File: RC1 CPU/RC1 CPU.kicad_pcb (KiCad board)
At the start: 2 copper layers, 99.1 x 99.1 mm, 51 parts, among them J1 Expansion, J2 RC1_UI_Port, J3 BARREL_JACK, M1 Mounting, M2 Mounting, M3 Mounting, M4 Mounting, U1 WD65C02, U2 HM62256BLP-7, U3 28C256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

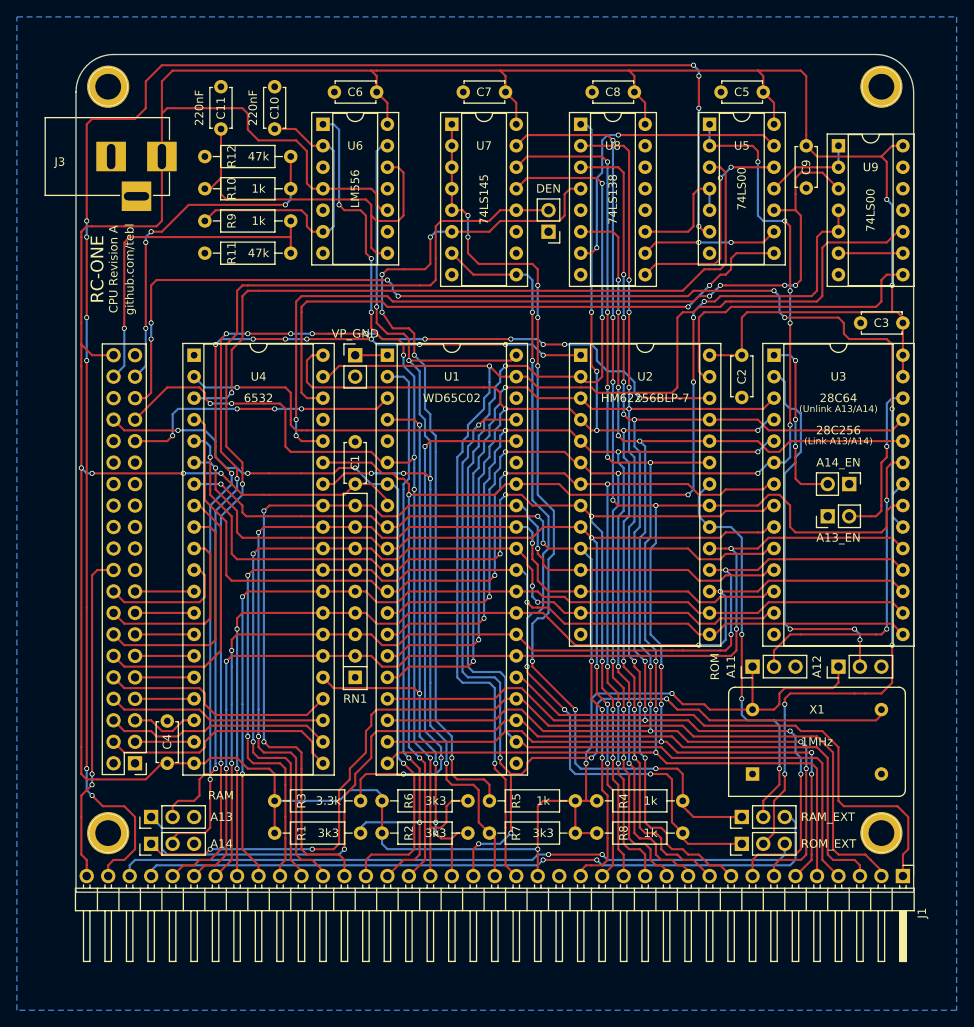
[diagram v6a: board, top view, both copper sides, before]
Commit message: Decided to connect remaining RAM address lines for external logic.
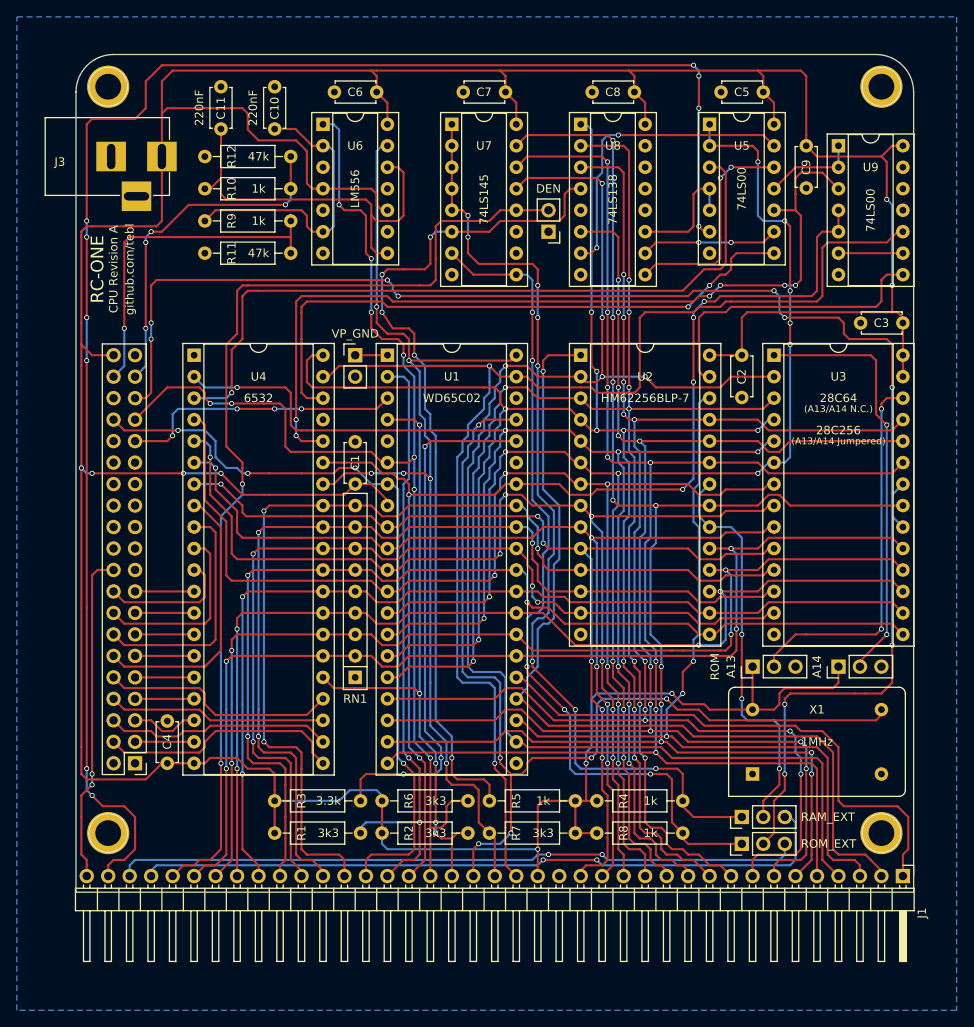
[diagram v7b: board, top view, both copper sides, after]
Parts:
- removed JP10: A14, Pin_Headers:Pin_Header_Straight_1x03_Pitch2.54mm
- removed JP5: A13_EN, Pin_Headers:Pin_Header_Straight_1x02_Pitch2.54mm
- removed JP6: A14_EN, Pin_Headers:Pin_Header_Straight_1x02_Pitch2.54mm
- removed JP9: A13, Pin_Headers:Pin_Header_Straight_1x03_Pitch2.54mm
- JP7: value A11 -> A13
- JP8: value A12 -> A14
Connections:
- JP7 pad 2: /A11_W -> Net-(JP7-Pad2)
- JP8 pad 2: /A12_W -> Net-(JP8-Pad2)
- U2 pad 1: /A14_RAM -> /A14
- U2 pad 26: /A13_RAM -> /A13
- U3 pad 1: Net-(JP6-Pad2) -> Net-(JP8-Pad2)
- U3 pad 2: /A12_W -> /A12
- U3 pad 23: /A11_W -> /A11
- U3 pad 26: Net-(JP5-Pad2) -> Net-(JP7-Pad2)
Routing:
- net /A13_RAM: track 125.3 -> 0.00 mm, vias 12 -> 0
- net /A14_RAM: track 108.8 -> 0.00 mm, vias 10 -> 0
- net Net-(JP8-Pad2): track 0.00 -> 50.4 mm, vias 0 -> 2
- net Net-(JP7-Pad2): track 0.00 -> 45.4 mm, vias 0 -> 2
- net /A12_W: track 45.3 -> 0.00 mm, vias 3 -> 0
- net /A11_W: track 38.1 -> 0.00 mm, vias 2 -> 0
- net /A11: track 158.7 -> 182.6 mm
- net /A12: track 148.2 -> 170.2 mm, vias 3 -> 5
- net Net-(JP6-Pad2): track 20.8 -> 0.00 mm, vias 3 -> 0
- net Net-(JP5-Pad2): track 19.8 -> 0.00 mm, vias 1 -> 0
- net /A13: track 114.7 -> 98.7 mm, vias 1 -> 3
- net /A14: track 117.0 -> 106.9 mm, vias 2 -> 1
- net /A10: track 192.1 -> 186.9 mm
- net /R/~W: track 143.1 -> 142.3 mm
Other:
- board text added: "(A13/A14 Jumpered)"
- board text added: "(A13/A14 N.C.)"
- board text removed: "(Link A13/A14)"
- board text removed: "(Unlink A13/A14)"
- board text removed: "A13"
- board text removed: "A14"
- board text removed: "RAM"
